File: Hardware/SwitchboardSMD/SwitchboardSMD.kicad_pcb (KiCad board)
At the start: 2 copper layers, 70 x 40 mm, 40 parts, among them J2 S88_In_Plug, J4 S88_Out_Plug, Q1 BC237, SW1 SW_Push, SW2 SW_Push, SW3 SW_Push, SW4 SW_Push, SW5 SW_Push, SW6 SW_Push, SW7 SW_Push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

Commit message: Updated to v1.3 for manufacturing
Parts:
- removed RN1, RN2: 100k, Resistor_THT:R_Array_SIP5
- added R14: 100k, Resistor_SMD:R_1206_3216Metric_Pad1.30x1.75mm_HandSolder, F.Cu at (31.5, 33.0)
- added R15: 100k, Resistor_SMD:R_1206_3216Metric_Pad1.30x1.75mm_HandSolder, F.Cu at (31.5, 41.0)
- added R16: 100k, Resistor_SMD:R_1206_3216Metric_Pad1.30x1.75mm_HandSolder, F.Cu at (43.0, 33.0)
- added R17: 100k, Resistor_SMD:R_1206_3216Metric_Pad1.30x1.75mm_HandSolder, F.Cu at (44.0, 41.0)
- added R18: 100k, Resistor_SMD:R_1206_3216Metric_Pad1.30x1.75mm_HandSolder, F.Cu at (63.0, 33.0)
- added R19: 100k, Resistor_SMD:R_1206_3216Metric_Pad1.30x1.75mm_HandSolder, F.Cu at (61.5, 41.0)
- added R20: 100k, Resistor_SMD:R_1206_3216Metric_Pad1.30x1.75mm_HandSolder, F.Cu at (76.0, 33.0)
- added R21: 100k, Resistor_SMD:R_1206_3216Metric_Pad1.30x1.75mm_HandSolder, F.Cu at (76.0, 41.0)
- C1, C2, C3, C4, C5, C6, C7, C8, C9: footprint Capacitor_THT:C_Disc_D3.4mm_W2.1mm_P2.50mm -> Capacitor_SMD:C_1206_3216Metric
- J2: footprint Connector_PinSocket_2.00mm:PinSocket_1x06_P2.00mm_Horizontal -> Connector_PinSocket_2.54mm:PinSocket_1x06_P2.54mm_Horizontal
- J4: footprint Connector_PinHeader_2.00mm:PinHeader_1x06_P2.00mm_Horizontal -> Connector_PinHeader_2.54mm:PinHeader_1x06_P2.54mm_Horizontal
- Q1: value BC237 -> MMBT5551L; footprint Package_TO_SOT_THT:TO-92_Inline -> Package_TO_SOT_SMD:SOT-23
- R1, R10, R11, R2, R3, R4, R5, R6, R7, R8, R9: footprint Resistor_THT:R_Axial_DIN0204_L3.6mm_D1.6mm_P7.62mm_Horizontal -> Resistor_SMD:R_1206_3216Metric_Pad1.30x1.75mm_HandSolder
- U1, U2, U3: footprint Package_SO:SOIC-16_3.9x9.9mm_P1.27mm -> Package_SO:TSSOP-16_4.4x5mm_P0.65mm
- moved H4 66.5 mm to (83.5, 50.5)
- moved H2 64.8 mm to (22.5, 50.5)
- moved H1 34.5 mm to (22.5, 22.5)
- moved R2 28.9 mm to (50.0, 41.0), turned to 90 degrees
- moved Q1 20.0 mm to (51.1, 47.5), turned to 0 degrees
- moved R3 18.2 mm to (53.5, 43.0), turned to -90 degrees
- moved C9 13.8 mm to (80.0, 39.5)
- moved C4 12.4 mm to (38.0, 48.0), turned to -90 degrees
- moved C8 12.0 mm to (71.0, 48.0), turned to -90 degrees
- moved C2 9.70 mm to (35.5, 48.0), turned to -90 degrees
- moved C7 9.52 mm to (70.5, 24.5), turned to 90 degrees
- moved R1 9.18 mm to (56.0, 44.5)
- moved C6 8.34 mm to (67.5, 48.0), turned to -90 degrees
- moved C1 8.24 mm to (35.5, 25.0), turned to 90 degrees
- moved C3 7.07 mm to (38.0, 25.0), turned to 90 degrees
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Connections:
- Q1 pad 1: /RESET_LOCAL -> Net-(Q1-C)
- Q1 pad 2: Net-(Q1-Pad2) -> GND
- Q1 pad 3: GND -> /RESET_LOCAL
- R2 pad 1: Net-(Q1-Pad2) -> Net-(Q1-C)
- U1 pad 16: VCC -> GND
- U1 pad 8: GND -> unconnected-(U1-Vss-Pad8)
- U2 pad 16: VCC -> GND
- U2 pad 8: GND -> unconnected-(U2-Vss-Pad8)
- U3 pad 12: (no net) -> unconnected-(U3-Q6-Pad12)
- U3 pad 2: (no net) -> unconnected-(U3-Q5-Pad2)
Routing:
- net GND: track 0.00 -> 298.6 mm, vias 21 -> 11
- net Net-(C8-Pad1): track 41.2 -> 1.98 mm
- net VCC: track 153.9 -> 121.2 mm, vias 6 -> 8
- net Net-(C1-Pad1): track 43.6 -> 11.6 mm
- net Net-(C7-Pad1): track 41.3 -> 15.5 mm
- net Net-(C2-Pad1): track 34.6 -> 11.1 mm
- net /RESET: track 82.0 -> 60.6 mm, vias 0 -> 1
- net Net-(C3-Pad1): track 31.8 -> 12.3 mm
- net Net-(C5-Pad1): track 29.4 -> 13.5 mm
- net /RESET_LOCAL: track 94.9 -> 81.0 mm, vias 1 -> 0
- net Net-(C6-Pad1): track 21.2 -> 12.5 mm
- net Net-(C4-Pad1): track 21.6 -> 13.0 mm
- net /DATA_IN: track 43.4 -> 38.0 mm, vias 0 -> 2
- net /LOAD: track 65.6 -> 60.6 mm
- net Net-(U3-P1): track 25.6 -> 21.1 mm
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- removed copper zone on B.Cu, net GND
- removed copper zone on F.Cu, net GND
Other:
- board size 70 x 40 mm -> 66 x 33 mm
- net class Default removed
- net class Power removed
- board text added: "CLK"
- board text added: "DATA"
- board text added: "GND"
- board text added: "LOAD"
- board text added: "RST"
- board text added: "Switchbaord v1.3"
- board text added: "VCC"
- board text removed: "DATA GND CLK LD RES VCC"
- board text removed: "In"
- board text removed: "Out"
- board text removed: "RR32Can"
- board text removed: "Switchboard v1.1"

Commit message: Updated Geometry
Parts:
- J2: value S88_In_Plug -> S88_In
- J4: value S88_Out_Plug -> S88_Out
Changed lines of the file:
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@@
 	(net 27 "unconnected-(U3-Q6-Pad12)")
 	(net 28 "unconnected-(U3-Q5-Pad2)")
-	(net 29 "Net-(Q1-C)")
+	(net 29 "Net-(Q1-B)")
 	(net 30 "Net-(C1-Pad1)")
 	(net 31 "Net-(C2-Pad1)")
@@
 		(tags "tact sw push 6mm")
 		(property "Reference" "SW8"
-			(at 3.25 -2 90)
+			(at 8.5 2.25 180)
 			(layer "F.SilkS")
 			(effects
@@
 		(tags "capacitor")
 		(property "Reference" "C4"
-			(at 0 -1.85 90)
+			(at 3.5 0 90)
 			(layer "F.SilkS")
 			(effects
@@
 		(tags "capacitor")
 		(property "Reference" "C7"
-			(at 0 -1.85 90)
+			(at 3.25 0 90)
 			(layer "F.SilkS")
 			(effects
@@
 		(tags "tact sw push 6mm")
 		(property "Reference" "SW5"
-			(at 3.25 -2 90)
+			(at 8 2.25 180)
 			(layer "F.SilkS")
 			(effects
@@
 		(tags "capacitor")
 		(property "Reference" "C2"
-			(at 0 -1.85 90)
+			(at 3.5 0 90)
 			(layer "F.SilkS")
 			(effects
@@
 		(tags "tact sw push 6mm")
 		(property "Reference" "SW7"
-			(at 3.25 -2 90)
+			(at -1.5 2.25 180)
 			(layer "F.SilkS")
 			(effects
@@
 		(tags "tact sw push 6mm")
 		(property "Reference" "SW6"
-			(at 3.25 -2 90)
+			(at -2 2.5 180)
 			(layer "F.SilkS")
 			(effects
@@
 			(layers "F.Cu" "F.Mask" "F.Paste")
 			(roundrect_rratio 0.192308)
-			(net 29 "Net-(Q1-C)")
+			(net 29 "Net-(Q1-B)")
 			(pintype "passive")
 		)
@@
 		(tags "capacitor")
 		(property "Reference" "C8"
-			(at 0 -1.85 90)
+			(at 3.5 0 90)
 			(layer "F.SilkS")
 			(effects
@@
 		(tags "tact sw push 6mm")
 		(property "Reference" "SW4"
-			(at 3.25 -2 90)
+			(at 8.5 2 180)
 			(layer "F.SilkS")
 			(effects
@@
 		(tags "capacitor")
 		(property "Reference" "C3"
-			(at 0 -1.85 90)
+			(at 3.5 0 90)
 			(layer "F.SilkS")
 			(effects
@@
 		(tags "tact sw push 6mm")
 		(property "Reference" "SW1"
-			(at 3.25 -2 90)
+			(at 8 2.25 180)
 			(layer "F.SilkS")
 			(effects
@@
 		(tags "capacitor")
 		(property "Reference" "C1"
-			(at 0 -1.85 90)
+			(at 3.5 0 90)
 			(layer "F.SilkS")
 			(effects
@@
 		(tags "tact sw push 6mm")
 		(property "Reference" "SW3"
-			(at 3.25 -2 90)
+			(at -1.5 2.25 180)
 			(layer "F.SilkS")
 			(effects
@@
 		(tags "capacitor")
 		(property "Reference" "C5"
-			(at 0 -1.85 90)
+			(at 3.225 0 90)
 			(layer "F.SilkS")
 			(effects
@@
 			(layers "F.Cu" "F.Mask" "F.Paste")
 			(roundrect_rratio 0.25)
-			(net 29 "Net-(Q1-C)")
+			(net 29 "Net-(Q1-B)")
 			(pinfunction "B")
 			(pintype "input")
@@
 			(at -4.38 -2.77 0)
 			(layer "F.SilkS")
+			(hide yes)
 			(effects
 				(font
@@
 			)
 		)
-		(property "Value" "S88_In_Plug"
-			(at -4.38 15.47 0)
-			(layer "F.Fab")
+		(property "Value" "S88_In"
+			(at -2.75 16.821282 0)
+			(layer "F.SilkS")
 			(effects
 				(font
@@
 		(tags "tact sw push 6mm")
 		(property "Reference" "SW2"
-			(at 3.25 -2 90)
+			(at -2 2.5 180)
 			(layer "F.SilkS")
 			(effects
@@
 		(tags "capacitor")
 		(property "Reference" "C6"
-			(at 0 -1.85 90)
+			(at 3.5 0 90)
 			(layer "F.SilkS")
 			(effects
@@
 			(at 4.385 -2.27 0)
 			(layer "F.SilkS")
+			(hide yes)
 			(effects
 				(font
@@
 			)
 		)
-		(property "Value" "S88_Out_Plug"
-			(at 4.385 14.97 0)
-			(layer "F.Fab")
+		(property "Value" "S88_Out"
+			(at 1.75 15.321282 0)
+			(layer "F.SilkS")
 			(effects
 				(font

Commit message: Fix VCC/GND assignment
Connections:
- U1 pad 16: GND -> VCC
- U1 pad 8: unconnected-(U1-Vss-Pad8) -> GND
- U2 pad 16: GND -> VCC
- U2 pad 8: unconnected-(U2-Vss-Pad8) -> GND
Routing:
- net VCC: track 121.2 -> 133.9 mm
- net GND: track 298.6 -> 311.3 mm, vias 11 -> 12

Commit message: Updated JLCPCB DRC
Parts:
- moved R6 0.54 mm to (38.0, 29.8)
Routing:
- net Net-(C8-Pad1): track 1.98 -> 17.0 mm
- net Net-(C3-Pad1): track 12.3 -> 19.6 mm
- net Net-(C4-Pad1): track 13.0 -> 19.5 mm
- net Net-(C2-Pad1): track 11.1 -> 17.6 mm
- net Net-(C1-Pad1): track 11.6 -> 18.1 mm
- net Net-(C6-Pad1): track 12.5 -> 19.0 mm
- net Net-(C5-Pad1): track 13.5 -> 20.0 mm
- net Net-(C7-Pad1): track 15.5 -> 20.0 mm
- net VCC: track 133.9 -> 129.9 mm, vias 8 -> 9
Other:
- board text added: "IN"
- board text added: "OUT"

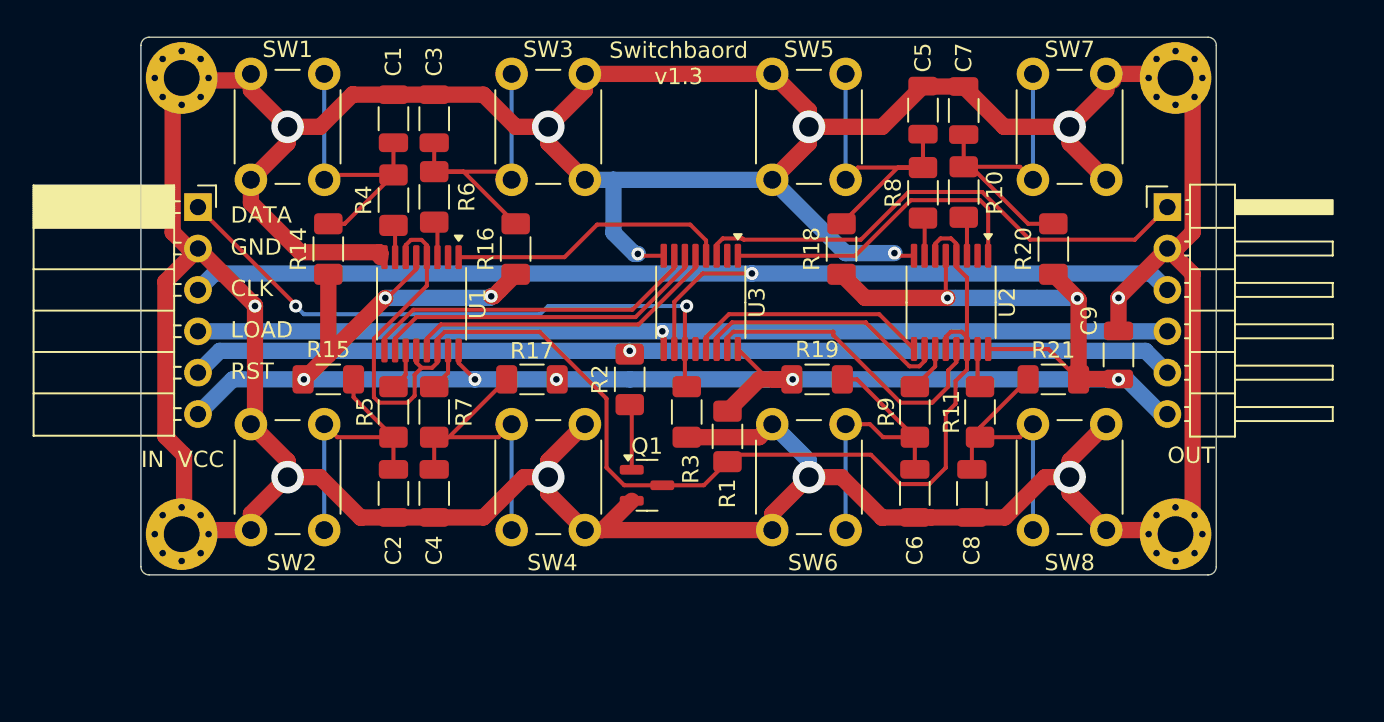
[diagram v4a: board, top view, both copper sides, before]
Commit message: Center connectors
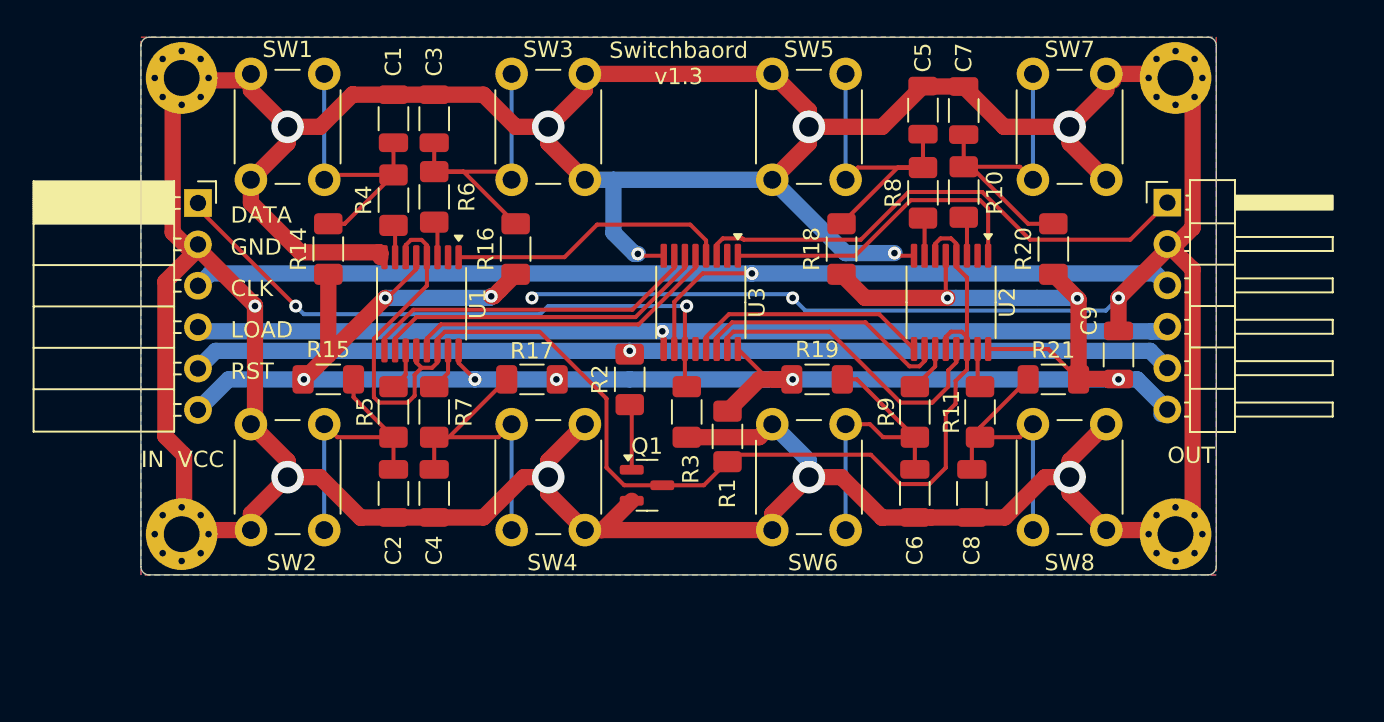
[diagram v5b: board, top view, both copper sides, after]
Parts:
- moved J4 0.28 mm to (83.0, 30.1)
- moved J2 0.25 mm to (23.5, 30.2)
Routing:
- net GND: track 311.3 -> 350.1 mm, vias 12 -> 14
- net /LOAD: track 60.6 -> 61.7 mm
- added copper zone on B.Cu, net GND
- added copper zone on F.Cu, net GND

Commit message: Updated production files
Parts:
- H1, H2, H3, H4: footprint MountingHole:MountingHole_2.2mm_M2_Pad_Via -> MountingHole:MountingHole_2.2mm_M2
- moved H1 1.41 mm to (21.5, 21.5)
- moved H2 1.41 mm to (21.5, 51.5)
- moved H3 1.41 mm to (84.5, 21.5)
- moved H4 1.41 mm to (84.5, 51.5)
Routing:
- net GND: track 350.1 -> 265.6 mm, vias 14 -> 21

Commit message: Files as sent for production
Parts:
- added H5: MountingHole_Pad, MountingHole:MountingHole_3.2mm_M3_Pad_Via, F.Cu at (53.0, 27.5)
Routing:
- net GND: track 265.6 -> 267.2 mm
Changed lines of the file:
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@@
 		)
 	)
+	(footprint "MountingHole:MountingHole_3.2mm_M3_Pad_Via"
+		(layer "F.Cu")
+		(at 53 27.5)
+		(descr "Mounting Hole 3.2mm, M3, generated by kicad-footprint-generator mountinghole.py")
+		(tags "mountinghole M3")
+		(property "Reference" "H5"
+			(at 0 -4.15 0)
+			(layer "F.SilkS")
+			(hide yes)
+			(effects
+				(font
+					(size 1 1)
+					(thickness 0.15)
+				)
+			)
+		)
+		(property "Value" "MountingHole_Pad"
+			(at 0 4.15 0)
+			(layer "F.Fab")
+			(hide yes)
+			(effects
+				(font
+					(size 1 1)
+					(thickness 0.15)
+				)
+			)
+		)
+		(property "Datasheet" "~"
+			(at 0 0 0)
+			(layer "F.Fab")
+			(hide yes)
+			(effects
+				(font
+					(size 1.27 1.27)
+					(thickness 0.15)
+				)
+			)
+		)
+		(property "Description" ""
+			(at 0 0 0)
+			(layer "F.Fab")
+			(hide yes)
+			(effects
+				(font
+					(size 1.27 1.27)
+					(thickness 0.15)
+				)
+			)
+		)
+		(property ki_fp_filters "MountingHole*Pad*")
+		(sheetname "/")
+		(sheetfile "SwitchboardSMD.kicad_sch")
+		(attr exclude_from_pos_files)
+		(fp_circle
+			(center 0 0)
+			(end 3.2 0)
+			(stroke
+				(width 0.15)
+				(type solid)
+			)
+			(fill no)
+			(layer "Cmts.User")
+		)
+		(fp_circle
+			(center 0 0)
+			(end 3.45 0)
+			(stroke
+				(width 0.05)
+				(type solid)
+			)
+			(fill no)
+			(layer "F.CrtYd")
+		)
+		(fp_text user "${REFERENCE}"
+			(at 0 0 0)
+			(layer "F.Fab")
+			(effects
+				(font
+					(size 1 1)
+					(thickness 0.15)
+				)
+			)
+		)
+		(pad "1" thru_hole circle
+			(at -2.4 0)
+			(size 0.8 0.8)
+			(drill 0.5)
+			(layers "*.Cu" "*.Mask")
+			(remove_unused_layers no)
+			(net 1 "GND")
+			(pinfunction "1")
+			(pintype "input")
+			(zone_connect 2)
+		)
+		(pad "1" thru_hole circle
+			(at -1.697056 -1.697056)
+			(size 0.8 0.8)
+			(drill 0.5)
+			(layers "*.Cu" "*.Mask")
+			(remove_unused_layers no)
+			(net 1 "GND")
+			(pinfunction "1")
+			(pintype "input")
+			(zone_connect 2)
+		)
+		(pad "1" thru_hole circle
+			(at -1.697056 1.697056)
+			(size 0.8 0.8)
+			(drill 0.5)
+			(layers "*.Cu" "*.Mask")
+			(remove_unused_layers no)
+			(net 1 "GND")
+			(pinfunction "1")
+			(pintype "input")
+			(zone_connect 2)
+		)
+		(pad "1" thru_hole circle
+			(at 0 -2.4)
+			(size 0.8 0.8)
+			(drill 0.5)
+			(layers "*.Cu" "*.Mask")
+			(remove_unused_layers no)
+			(net 1 "GND")
+			(pinfunction "1")
+			(pintype "input")
+			(zone_connect 2)
+		)
+		(pad "1" thru_hole circle
+			(at 0 0)
+			(size 6.4 6.4)
+			(drill 3.2)
+			(layers "*.Cu" "*.Mask")
+			(remove_unused_layers no)
+			(net 1 "GND")
+			(pinfunction "1")
+			(pintype "input")
+			(zone_connect 2)
+		)
+		(pad "1" thru_hole circle
+			(at 0 2.4)
+			(size 0.8 0.8)
+			(drill 0.5)
+			(layers "*.Cu" "*.Mask")
+			(remove_unused_layers no)
+			(net 1 "GND")
+			(pinfunction "1")
+			(pintype "input")
+			(zone_connect 2)
+		)
+		(pad "1" thru_hole circle
+			(at 1.697056 -1.697056)
+			(size 0.8 0.8)
+			(drill 0.5)
+			(layers "*.Cu" "*.Mask")
+			(remove_unused_layers no)
+			(net 1 "GND")
+			(pinfunction "1")
+			(pintype "input")
+			(zone_connect 2)
+		)
+		(pad "1" thru_hole circle
+			(at 1.697056 1.697056)
+			(size 0.8 0.8)
+			(drill 0.5)
+			(layers "*.Cu" "*.Mask")
+			(remove_unused_layers no)
+			(net 1 "GND")
+			(pinfunction "1")
+			(pintype "input")
+			(zone_connect 2)
+		)
+		(pad "1" thru_hole circle
+			(at 2.4 0)
+			(size 0.8 0.8)
+			(drill 0.5)
+			(layers "*.Cu" "*.Mask")
+			(remove_unused_layers no)
+			(net 1 "GND")
+			(pinfunction "1")
+			(pintype "input")
+			(zone_connect 2)
+		)
+		(embedded_fonts no)
+	)
 	(footprint "Button_Switch_THT:SW_PUSH_6mm"
 		(layer "F.Cu")
@@
 	)
 	(segment
+		(start 55 25.5)
+		(end 53 27.5)
+		(width 1)
+		(layer "F.Cu")
+		(net 1)
+	)
+	(segment
 		(start 44.699 25.199)
 		(end 45 25.5)
@@
 	)
 	(segment
+		(start 51 25.5)
+		(end 53 27.5)
+		(width 1)
+		(layer "F.Cu")
+		(net 1)
+	)
+	(segment
 		(start 75.821 48.179)
 		(end 62.179 48.179)
@@
 	)
 	(segment
+		(start 45 25.5)
+		(end 51 25.5)
+		(width 1)
+		(layer "F.Cu")
+		(net 1)
+	)
+	(segment
 		(start 84.551 34.241)
 		(end 84.551 43.492446)
@@
 	)
 	(segment
-		(start 52.0875 33.4125)
-		(end 50.6135 33.4125)
-		(width 0.25)
+		(start 61 25.5)
+		(end 55 25.5)
+		(width 1)
 		(layer "F.Cu")
 		(net 1)
 	)
 	(segment
-		(start 45 25.5)
-		(end 61 25.5)
-		(width 1)
+		(start 52.0875 33.4125)
+		(end 50.6135 33.4125)
+		(width 0.25)
 		(layer "F.Cu")
 		(net 1)
